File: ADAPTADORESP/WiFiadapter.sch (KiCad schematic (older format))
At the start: 9 parts, among them J1 ADAP_ESP, U1 ESP8266-12E/ESP-12E

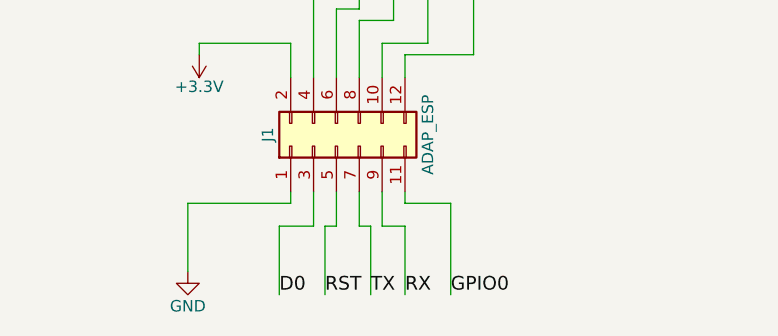
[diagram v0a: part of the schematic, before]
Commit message: PCBS_Adap_mon
Correxión del RX y TX del adaptador, PCB monitor doble capa.
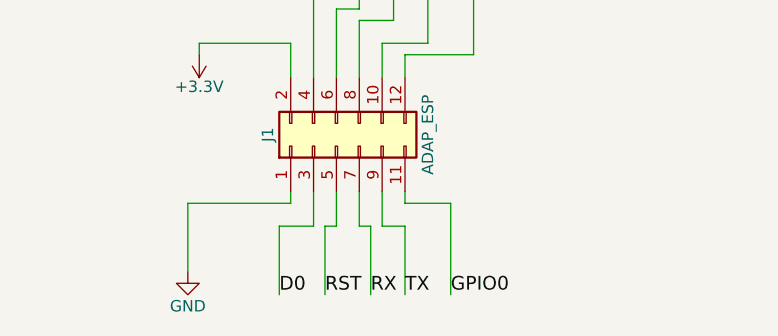
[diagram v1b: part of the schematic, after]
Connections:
- net RX: now also J1.7 (Pin_7); no longer J1.9 (Pin_9)
- net TX: now also J1.9 (Pin_9); no longer J1.7 (Pin_7)
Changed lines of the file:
@@
 Text Label 5600 3600 0    60   ~ 0
 SDA
+Text Label 5500 4900 0    60   ~ 0
+TX
 Text Label 5350 4900 0    60   ~ 0
-TX
-Text Label 5500 4900 0    60   ~ 0
 RX
 $Comp
